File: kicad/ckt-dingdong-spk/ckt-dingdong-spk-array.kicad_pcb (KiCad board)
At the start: 2 copper layers, 40.6 x 180.3 mm, 170 parts, among them J1 Conn_01x02_MountingPin

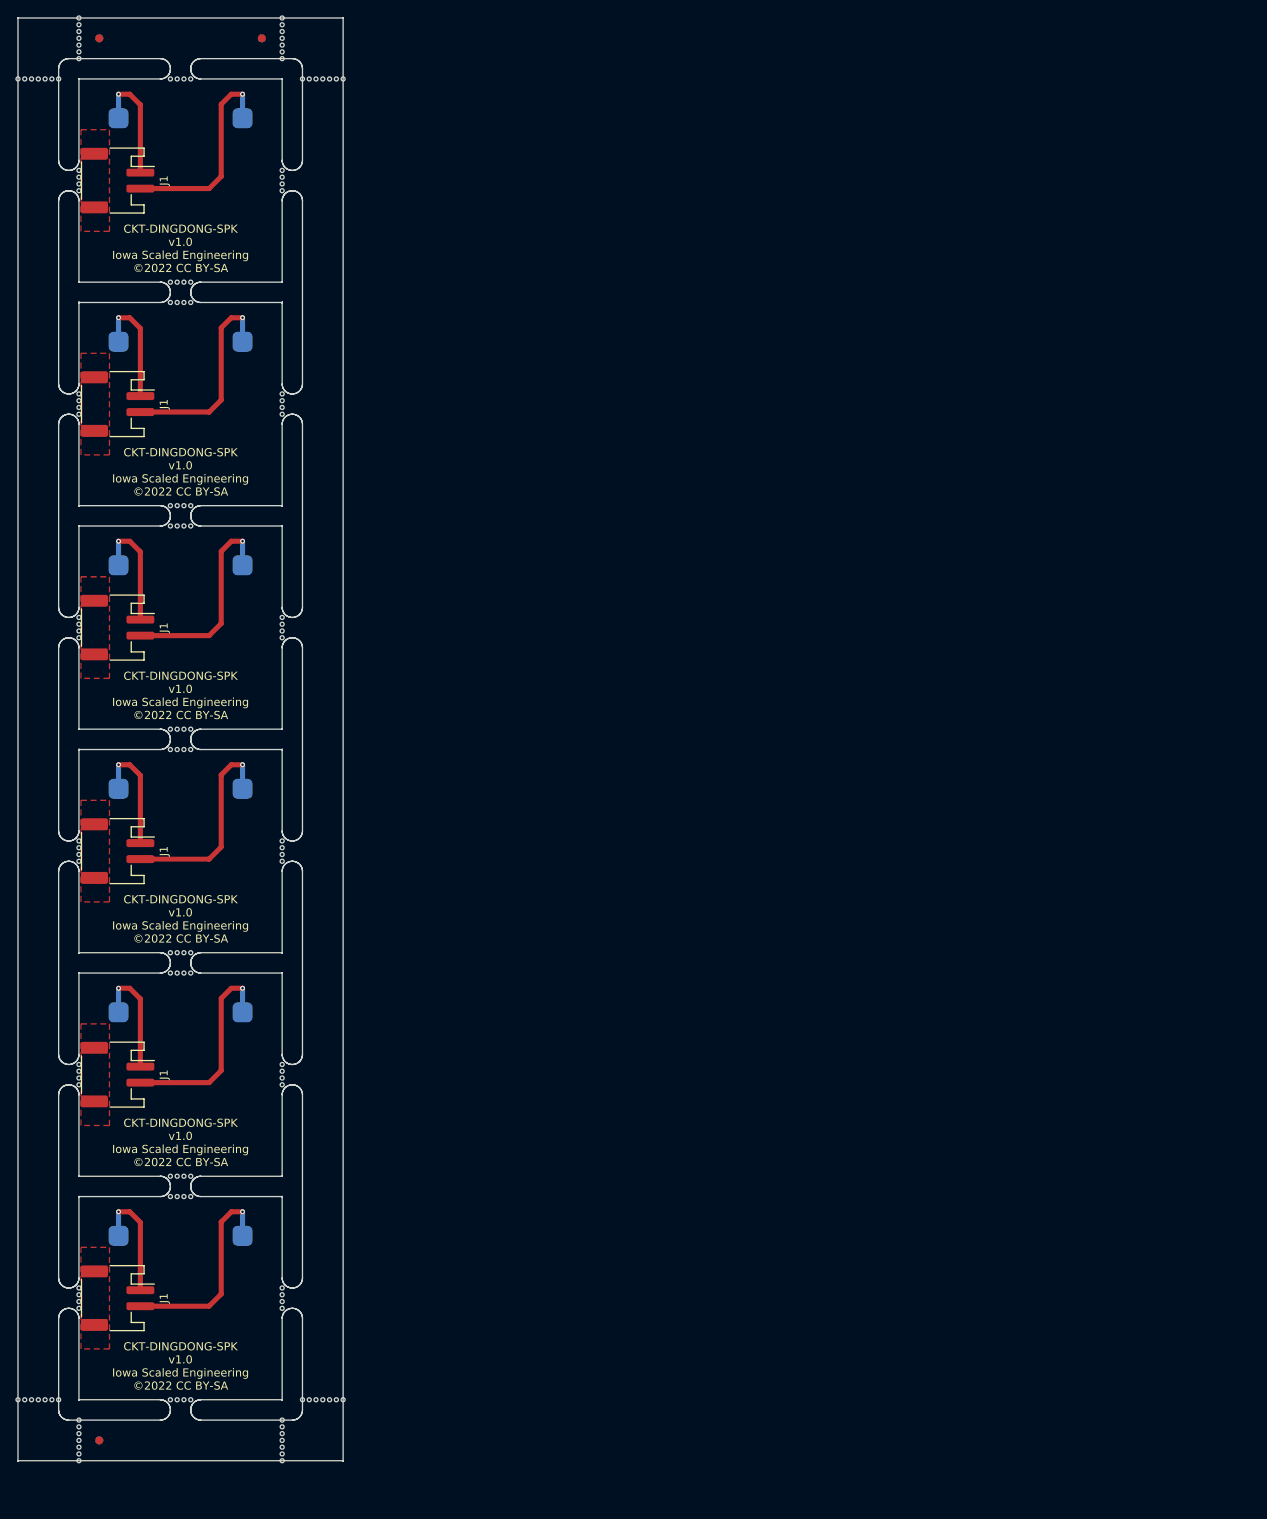
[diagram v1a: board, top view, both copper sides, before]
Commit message: Updated array with v2 board
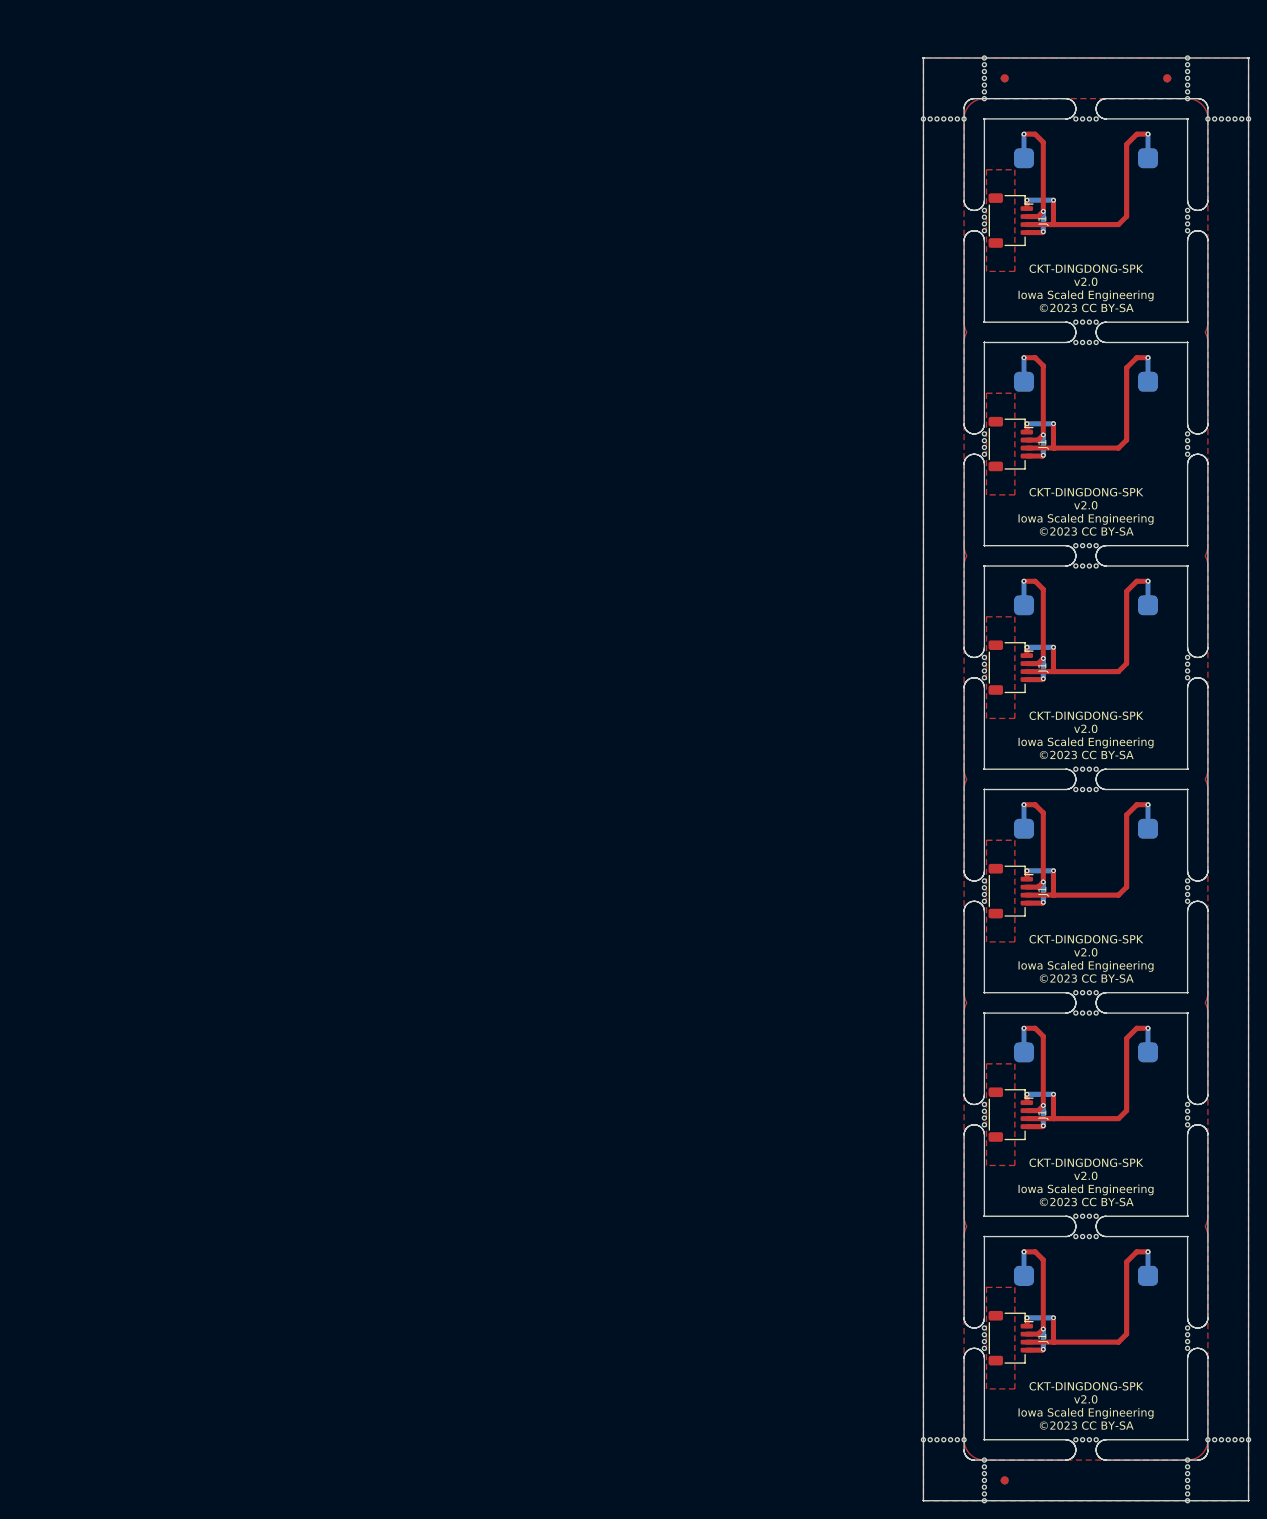
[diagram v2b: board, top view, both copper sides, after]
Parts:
- removed the J1 at (27.4, 35.3)
- removed the J1 at (27.4, 63.3)
- removed the J1 at (27.4, 147.1)
- removed the J1 at (27.4, 119.1)
- removed the J1 at (27.4, 175.0)
- removed the J1 at (27.4, 91.2)
- removed the REF** at (20.1, 22.6)
- removed the REF** at (53.9, 187.7)
- removed the REF** at (34.9, 134.4)
- removed the REF** at (45.5, 17.5) (x2)
- removed the REF** at (34.9, 76.0)
- removed the REF** at (34.9, 48.0)
- removed the REF** at (36.6, 48.0)
- removed the REF** at (52.3, 22.6)
- removed the REF** at (22.6, 194.5)
- removed the REF** at (22.6, 118.7)
- removed the REF** at (35.7, 187.7)
- removed the REF** at (48.0, 191.1)
- removed the REF** at (22.6, 147.5)
- removed the REF** at (55.6, 187.7)
- removed the REF** at (48.0, 194.5)
- removed the REF** at (36.6, 162.3)
- removed the REF** at (17.5, 22.6)
- removed the REF** at (36.6, 22.6)
- removed the REF** at (34.9, 106.4)
- removed the REF** at (48.0, 120.4)
- removed the REF** at (48.0, 18.4)
- removed the REF** at (34.0, 134.4)
- removed the REF** at (22.6, 36.6)
- removed the REF** at (22.6, 92.5)
- removed the REF** at (17.5, 187.7)
- removed the REF** at (48.0, 192.0)
- removed the REF** at (22.6, 34.0)
- removed the REF** at (53.9, 22.6)
- removed the REF** at (19.2, 187.7)
- removed the REF** at (34.0, 159.8)
- removed the REF** at (36.6, 50.6)
- removed the REF** at (22.6, 174.6)
- removed the REF** at (48.0, 90.8)
- removed the REF** at (22.6, 191.1)
- removed the REF** at (34.9, 159.8)
- removed the REF** at (18.4, 22.6)
- removed the REF** at (15.0, 187.7)
- removed the REF** at (22.6, 146.7)
- removed the REF** at (34.9, 187.7)
- removed the REF** at (22.6, 62.0)
- removed the REF** at (15.8, 22.6)
- removed the REF** at (34.9, 131.8)
- removed the REF** at (48.0, 92.5)
- removed the REF** at (22.6, 34.9)
- removed the REF** at (36.6, 78.5)
- removed the REF** at (35.7, 22.6)
- removed the REF** at (22.6, 119.6)
- removed the REF** at (22.6, 175.4)
- removed the REF** at (48.0, 15.0)
- removed the REF** at (35.7, 50.6)
- removed the REF** at (50.6, 22.6)
- removed the REF** at (22.6, 18.4)
- removed the REF** at (48.0, 190.3)
- removed the REF** at (35.7, 78.5)
- removed the REF** at (19.2, 22.6)
- removed the REF** at (34.0, 106.4)
- removed the REF** at (51.4, 187.7)
- removed the REF** at (48.0, 176.3)
- removed the REF** at (22.6, 176.3)
- removed the REF** at (34.9, 50.6)
- removed the REF** at (34.0, 50.6)
- removed the REF** at (22.6, 35.7)
- removed the REF** at (36.6, 159.8)
- removed the REF** at (25.2, 192.8) (x2)
- removed the REF** at (25.2, 17.5) (x2)
- removed the REF** at (36.6, 106.4)
- removed the REF** at (34.9, 78.5)
- removed the REF** at (35.7, 131.8)
- removed the REF** at (48.0, 35.7)
- removed the REF** at (35.7, 48.0)
- removed the REF** at (35.7, 162.3)
- removed the REF** at (48.0, 20.1)
- removed the REF** at (48.0, 147.5)
- removed the REF** at (22.6, 120.4)
- removed the REF** at (34.0, 78.5)
- removed the REF** at (22.6, 195.3)
- removed the REF** at (52.3, 187.7)
- removed the REF** at (36.6, 76.0)
- removed the REF** at (22.6, 15.8)
- removed the REF** at (16.7, 22.6)
- removed the REF** at (22.6, 193.6)
- removed the REF** at (15.8, 187.7)
- removed the REF** at (15.0, 22.6)
- removed the REF** at (48.0, 17.5)
- removed the REF** at (48.0, 118.7)
- removed the REF** at (54.8, 187.7)
- removed the REF** at (16.7, 187.7)
- removed the REF** at (22.6, 19.2)
- removed the REF** at (48.0, 62.8)
- removed the REF** at (22.6, 15.0)
- removed the REF** at (48.0, 64.5)
- removed the REF** at (20.1, 187.7)
- removed the REF** at (53.1, 22.6)
- removed the REF** at (22.6, 64.5)
- removed the REF** at (48.0, 36.6)
- removed the REF** at (36.6, 131.8)
- removed the REF** at (48.0, 173.8)
- removed the REF** at (36.6, 187.7)
- removed the REF** at (35.7, 106.4)
- removed the REF** at (22.6, 63.7)
- removed the REF** at (36.6, 103.9)
- removed the REF** at (35.7, 159.8)
- removed the REF** at (22.6, 192.0)
- removed the REF** at (48.0, 148.3)
- removed the REF** at (22.6, 91.6)
- removed the REF** at (22.6, 62.8)
- removed the REF** at (54.8, 22.6)
- removed the REF** at (48.0, 62.0)
- removed the REF** at (34.0, 22.6)
- removed the REF** at (48.0, 16.7)
- removed the REF** at (34.0, 162.3)
- removed the REF** at (48.0, 34.0)
- removed the REF** at (34.0, 103.9)
- removed the REF** at (36.6, 134.4)
- removed the REF** at (48.0, 34.9)
- removed the REF** at (48.0, 89.9)
- removed the REF** at (35.7, 134.4)
- removed the REF** at (48.0, 19.2)
- removed the REF** at (34.0, 76.0)
- removed the REF** at (18.4, 187.7)
- removed the REF** at (34.0, 187.7)
- removed the REF** at (22.6, 145.8)
- removed the REF** at (50.6, 187.7)
- removed the REF** at (35.7, 103.9)
- removed the REF** at (22.6, 17.5)
- removed the REF** at (48.0, 193.6)
- removed the REF** at (34.0, 48.0)
- removed the REF** at (48.0, 174.6)
- removed the REF** at (34.0, 131.8)
- removed the REF** at (35.7, 76.0)
- removed the REF** at (48.0, 119.6)
- removed the REF** at (22.6, 89.9)
- removed the REF** at (22.6, 192.8)
- removed the REF** at (48.0, 195.3)
- removed the REF** at (34.9, 22.6)
- removed the REF** at (48.0, 145.8)
- removed the REF** at (48.0, 63.7)
- removed the REF** at (22.6, 16.7)
- removed the REF** at (48.0, 15.8)
- removed the REF** at (22.6, 117.9)
- removed the REF** at (22.6, 173.8)
- removed the REF** at (53.1, 187.7)
- removed the REF** at (48.0, 91.6)
- removed the REF** at (22.6, 20.1)
- removed the REF** at (34.9, 103.9)
- removed the REF** at (34.9, 162.3)
- removed the REF** at (22.6, 148.3)
- removed the REF** at (48.0, 175.4)
- removed the REF** at (51.4, 22.6)
- removed the REF** at (48.0, 146.7)
- removed the REF** at (22.6, 190.3)
- removed the REF** at (55.6, 22.6)
- removed the REF** at (48.0, 117.9)
- removed the REF** at (48.0, 192.8)
- removed the REF** at (22.6, 90.8)
- removed the SPK1 at (35.3, 60.7)
- removed the SPK1 at (35.3, 116.6)
- removed the SPK1 at (35.3, 172.5)
- removed the SPK1 at (35.3, 32.8)
- removed the SPK1 at (35.3, 144.5)
- removed the SPK1 at (35.3, 88.7)
- added J1: SM04B-SRSS, Connector_JST:JST_SH_SM04B-SRSS-TB_1x04-1MP_P1.00mm_Horizontal, F.Cu at (139.1, 40.3)
- added J1: SM04B-SRSS, Connector_JST:JST_SH_SM04B-SRSS-TB_1x04-1MP_P1.00mm_Horizontal, F.Cu at (139.1, 152.1)
- added J1: SM04B-SRSS, Connector_JST:JST_SH_SM04B-SRSS-TB_1x04-1MP_P1.00mm_Horizontal, F.Cu at (139.1, 124.1)
- added J1: SM04B-SRSS, Connector_JST:JST_SH_SM04B-SRSS-TB_1x04-1MP_P1.00mm_Horizontal, F.Cu at (139.1, 180.0)
- added J1: SM04B-SRSS, Connector_JST:JST_SH_SM04B-SRSS-TB_1x04-1MP_P1.00mm_Horizontal, F.Cu at (139.1, 96.2)
- added J1: SM04B-SRSS, Connector_JST:JST_SH_SM04B-SRSS-TB_1x04-1MP_P1.00mm_Horizontal, F.Cu at (139.1, 68.3)
- added REF**: NPTH, NPTH, F.Cu at (129.0, 192.7)
- added REF**: NPTH, NPTH, F.Cu at (149.8, 139.4)
- added REF**: NPTH, NPTH, F.Cu at (148.1, 81.0)
- added REF**: NPTH, NPTH, F.Cu at (148.1, 192.7)
- added REF**: NPTH, NPTH, F.Cu at (161.2, 97.5)
- added REF**: NPTH, NPTH, F.Cu at (135.8, 69.5)
- added REF**: NPTH, NPTH, F.Cu at (130.7, 27.6)
- added REF**: NPTH, NPTH, F.Cu at (135.8, 180.4)
- added REF**: NPTH, NPTH, F.Cu at (161.2, 151.7)
- added REF**: NPTH, NPTH, F.Cu at (148.1, 164.8)
- added REF**: NPTH, NPTH, F.Cu at (135.8, 97.5)
- added REF**: NPTH, NPTH, F.Cu at (133.3, 192.7)
- added REF**: NPTH, NPTH, F.Cu at (166.3, 192.7)
- added REF**: NPTH, NPTH, F.Cu at (161.2, 180.4)
- added REF**: NPTH, NPTH, F.Cu at (161.2, 181.3)
- added REF**: NPTH, NPTH, F.Cu at (135.8, 200.3)
- added REF**: NPTH, NPTH, F.Cu at (147.2, 55.6)
- added REF**: NPTH, NPTH, F.Cu at (149.8, 167.3)
- added REF**: NPTH, NPTH, F.Cu at (163.7, 192.7)
- added REF**: NPTH, NPTH, F.Cu at (135.8, 20.8)
- added REF**: NPTH, NPTH, F.Cu at (161.2, 40.7)
- added REF**: NPTH, NPTH, F.Cu at (161.2, 21.7)
- added REF**: NPTH, NPTH, F.Cu at (165.4, 192.7)
- added REF**: NPTH, NPTH, F.Cu at (161.2, 152.5)
- added REF**: NPTH, NPTH, F.Cu at (135.8, 24.2)
- added REF**: NPTH, NPTH, F.Cu at (135.8, 198.6)
- added REF**: NPTH, NPTH, F.Cu at (148.1, 83.5)
- added REF**: NPTH, NPTH, F.Cu at (148.9, 27.6)
- added REF**: NPTH, NPTH, F.Cu at (168.0, 192.7)
- added REF**: NPTH, NPTH, F.Cu at (148.9, 83.5)
- added REF**: NPTH, NPTH, F.Cu at (129.9, 27.6)
- added REF**: NPTH, NPTH, F.Cu at (135.8, 125.4)
- added REF**: NPTH, NPTH, F.Cu at (133.3, 27.6)
- added REF**: NPTH, NPTH, F.Cu at (135.8, 151.7)
- added REF**: NPTH, NPTH, F.Cu at (147.2, 83.5)
- added REF**: NPTH, NPTH, F.Cu at (135.8, 94.9)
- added REF**: NPTH, NPTH, F.Cu at (161.2, 20.0)
- added REF**: NPTH, NPTH, F.Cu at (128.2, 27.6)
- added REF**: NPTH, NPTH, F.Cu at (161.2, 150.8)
- added REF**: NPTH, NPTH, F.Cu at (135.8, 41.6)
- added REF**: NPTH, NPTH, F.Cu at (167.1, 27.6)
- added REF**: NPTH, NPTH, F.Cu at (167.1, 192.7)
- added REF**: NPTH, NPTH, F.Cu at (149.8, 192.7)
- added REF**: NPTH, NPTH, F.Cu at (135.8, 124.6)
- added REF**: NPTH, NPTH, F.Cu at (168.8, 192.7)
- added REF**: NPTH, NPTH, F.Cu at (161.2, 179.6)
- added REF**: NPTH, NPTH, F.Cu at (148.1, 139.4)
- added REF**: NPTH, NPTH, F.Cu at (161.2, 124.6)
- added REF**: NPTH, NPTH, F.Cu at (131.6, 27.6)
- added REF**: NPTH, NPTH, F.Cu at (131.6, 192.7)
- added REF**: NPTH, NPTH, F.Cu at (148.1, 53.0)
- added REF**: NPTH, NPTH, F.Cu at (135.8, 122.9)
- added REF**: NPTH, NPTH, F.Cu at (149.8, 53.0)
- added REF**: NPTH, NPTH, F.Cu at (168.8, 27.6)
- added REF**: NPTH, NPTH, F.Cu at (135.8, 179.6)
- added REF**: NPTH, NPTH, F.Cu at (161.2, 25.1)
- added REF**: NPTH, NPTH, F.Cu at (164.6, 192.7)
- added REF**: NPTH, NPTH, F.Cu at (148.1, 167.3)
- added REF**: NPTH, NPTH, F.Cu at (135.8, 39.9)
- added REF**: Fiducial, Fiducial, F.Cu at (138.3, 22.5)
- added REF**: NPTH, NPTH, F.Cu at (163.7, 27.6)
- added REF**: NPTH, NPTH, F.Cu at (165.4, 27.6)
- added REF**: NPTH, NPTH, F.Cu at (161.2, 67.0)
- added REF**: Fiducial, Fiducial, B.Cu at (138.3, 197.8)
- added REF**: Fiducial, Fiducial, B.Cu at (138.3, 22.5)
- added REF**: Fiducial, Fiducial, B.Cu at (158.7, 22.5)
- added REF**: NPTH, NPTH, F.Cu at (161.2, 20.8)
- added REF**: NPTH, NPTH, F.Cu at (135.8, 178.8)
- added REF**: NPTH, NPTH, F.Cu at (135.8, 153.3)
- added REF**: NPTH, NPTH, F.Cu at (168.0, 27.6)
- added REF**: NPTH, NPTH, F.Cu at (147.2, 136.8)
- added REF**: NPTH, NPTH, F.Cu at (161.2, 68.7)
- added REF**: NPTH, NPTH, F.Cu at (135.8, 150.8)
- added REF**: NPTH, NPTH, F.Cu at (161.2, 196.1)
- added REF**: NPTH, NPTH, F.Cu at (166.3, 27.6)
- added REF**: NPTH, NPTH, F.Cu at (148.9, 164.8)
- added REF**: NPTH, NPTH, F.Cu at (147.2, 139.4)
- added REF**: NPTH, NPTH, F.Cu at (161.2, 199.5)
- added REF**: NPTH, NPTH, F.Cu at (135.8, 68.7)
- added REF**: NPTH, NPTH, F.Cu at (135.8, 20.0)
- added REF**: NPTH, NPTH, F.Cu at (147.2, 192.7)
- added REF**: NPTH, NPTH, F.Cu at (161.2, 39.9)
- added REF**: NPTH, NPTH, F.Cu at (161.2, 67.8)
- added REF**: NPTH, NPTH, F.Cu at (129.9, 192.7)
- added REF**: NPTH, NPTH, F.Cu at (161.2, 22.5)
- added REF**: NPTH, NPTH, F.Cu at (161.2, 24.2)
- added REF**: NPTH, NPTH, F.Cu at (161.2, 94.9)
- added REF**: NPTH, NPTH, F.Cu at (148.9, 192.7)
- added REF**: NPTH, NPTH, F.Cu at (135.8, 67.8)
- added REF**: NPTH, NPTH, F.Cu at (149.8, 136.8)
- added REF**: NPTH, NPTH, F.Cu at (135.8, 39.0)
- added REF**: NPTH, NPTH, F.Cu at (161.2, 125.4)
- added REF**: NPTH, NPTH, F.Cu at (135.8, 96.6)
- added REF**: NPTH, NPTH, F.Cu at (135.8, 181.3)
- added REF**: NPTH, NPTH, F.Cu at (129.0, 27.6)
- added REF**: NPTH, NPTH, F.Cu at (149.8, 55.6)
- added REF**: Fiducial, Fiducial, F.Cu at (138.3, 197.8)
- added REF**: NPTH, NPTH, F.Cu at (147.2, 167.3)
- added REF**: NPTH, NPTH, F.Cu at (132.4, 27.6)
- added REF**: NPTH, NPTH, F.Cu at (148.9, 136.8)
- added REF**: NPTH, NPTH, F.Cu at (135.8, 195.3)
- added REF**: NPTH, NPTH, F.Cu at (149.8, 81.0)
- added REF**: NPTH, NPTH, F.Cu at (161.2, 69.5)
- added REF**: NPTH, NPTH, F.Cu at (161.2, 197.0)
- added REF**: NPTH, NPTH, F.Cu at (149.8, 83.5)
- added REF**: NPTH, NPTH, F.Cu at (161.2, 96.6)
- added REF**: NPTH, NPTH, F.Cu at (161.2, 39.0)
- added REF**: NPTH, NPTH, F.Cu at (148.1, 136.8)
- added REF**: NPTH, NPTH, F.Cu at (161.2, 41.6)
- added REF**: NPTH, NPTH, F.Cu at (135.8, 40.7)
- added REF**: NPTH, NPTH, F.Cu at (147.2, 108.9)
- added REF**: NPTH, NPTH, F.Cu at (161.2, 195.3)
- added REF**: NPTH, NPTH, F.Cu at (135.8, 22.5)
- added REF**: NPTH, NPTH, F.Cu at (148.9, 108.9)
- added REF**: NPTH, NPTH, F.Cu at (128.2, 192.7)
- added REF**: NPTH, NPTH, F.Cu at (148.1, 27.6)
- added REF**: NPTH, NPTH, F.Cu at (149.8, 164.8)
- added REF**: NPTH, NPTH, F.Cu at (161.2, 122.9)
- added REF**: NPTH, NPTH, F.Cu at (135.8, 21.7)
- added REF**: NPTH, NPTH, F.Cu at (147.2, 81.0)
- added REF**: NPTH, NPTH, F.Cu at (161.2, 178.8)
- added REF**: NPTH, NPTH, F.Cu at (135.8, 199.5)
- added REF**: NPTH, NPTH, F.Cu at (161.2, 200.3)
- added REF**: NPTH, NPTH, F.Cu at (148.9, 81.0)
- added REF**: NPTH, NPTH, F.Cu at (135.8, 23.4)
- added REF**: NPTH, NPTH, F.Cu at (161.2, 95.8)
- added REF**: NPTH, NPTH, F.Cu at (148.9, 53.0)
- added REF**: NPTH, NPTH, F.Cu at (149.8, 108.9)
- added REF**: NPTH, NPTH, F.Cu at (135.8, 197.0)
- added REF**: NPTH, NPTH, F.Cu at (148.1, 55.6)
- added REF**: NPTH, NPTH, F.Cu at (135.8, 197.8)
- added REF**: NPTH, NPTH, F.Cu at (164.6, 27.6)
- added REF**: NPTH, NPTH, F.Cu at (148.1, 108.9)
- added REF**: NPTH, NPTH, F.Cu at (135.8, 196.1)
- added REF**: NPTH, NPTH, F.Cu at (147.2, 164.8)
- added REF**: NPTH, NPTH, F.Cu at (148.9, 111.4)
- added REF**: NPTH, NPTH, F.Cu at (161.2, 197.8)
- added REF**: NPTH, NPTH, F.Cu at (161.2, 153.3)
- added REF**: NPTH, NPTH, F.Cu at (148.9, 167.3)
- added REF**: Fiducial, Fiducial, F.Cu at (158.7, 22.5)
- added REF**: NPTH, NPTH, F.Cu at (147.2, 53.0)
- added REF**: NPTH, NPTH, F.Cu at (135.8, 152.5)
- added REF**: NPTH, NPTH, F.Cu at (135.8, 25.1)
- added REF**: NPTH, NPTH, F.Cu at (147.2, 27.6)
- added REF**: NPTH, NPTH, F.Cu at (130.7, 192.7)
- added REF**: NPTH, NPTH, F.Cu at (161.2, 23.4)
- added REF**: NPTH, NPTH, F.Cu at (161.2, 123.7)
- added REF**: NPTH, NPTH, F.Cu at (132.4, 192.7)
- added REF**: NPTH, NPTH, F.Cu at (135.8, 123.7)
- added REF**: NPTH, NPTH, F.Cu at (147.2, 111.4)
- added REF**: NPTH, NPTH, F.Cu at (149.8, 111.4)
- added REF**: NPTH, NPTH, F.Cu at (148.9, 139.4)
- added REF**: NPTH, NPTH, F.Cu at (148.9, 55.6)
- added REF**: NPTH, NPTH, F.Cu at (161.2, 198.6)
- added REF**: NPTH, NPTH, F.Cu at (135.8, 67.0)
- added REF**: NPTH, NPTH, F.Cu at (149.8, 27.6)
- added REF**: NPTH, NPTH, F.Cu at (135.8, 95.8)
- added REF**: NPTH, NPTH, F.Cu at (148.1, 111.4)
- added SPK1: Speaker, ISE_Generic:Speaker_13x18, B.Cu at (148.5, 121.6)
- added SPK1: Speaker, ISE_Generic:Speaker_13x18, B.Cu at (148.5, 37.8)
- added SPK1: Speaker, ISE_Generic:Speaker_13x18, B.Cu at (148.5, 93.7)
- added SPK1: Speaker, ISE_Generic:Speaker_13x18, B.Cu at (148.5, 65.7)
- added SPK1: Speaker, ISE_Generic:Speaker_13x18, B.Cu at (148.5, 177.5)
- added SPK1: Speaker, ISE_Generic:Speaker_13x18, B.Cu at (148.5, 149.5)
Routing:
- net Board_5-Net-(SPK1-Pad1): track 25.9 -> 35.5 mm, vias 1 -> 3
- net Board_4-Net-(SPK1-Pad1): track 25.9 -> 35.5 mm, vias 1 -> 3
- net Board_2-Net-(SPK1-Pad1): track 25.9 -> 35.5 mm, vias 1 -> 3
- net Board_3-Net-(SPK1-Pad1): track 25.9 -> 35.5 mm, vias 1 -> 3
- net Board_1-Net-(SPK1-Pad1): track 25.9 -> 35.5 mm, vias 1 -> 3
- net Board_0-Net-(SPK1-Pad1): track 25.9 -> 35.5 mm, vias 1 -> 3
- net Board_3-Net-(SPK1-Pad2): track 14.7 -> 21.5 mm, vias 1 -> 3
- net Board_1-Net-(SPK1-Pad2): track 14.7 -> 21.5 mm, vias 1 -> 3
- net Board_4-Net-(SPK1-Pad2): track 14.7 -> 21.5 mm, vias 1 -> 3
- net Board_0-Net-(SPK1-Pad2): track 14.7 -> 21.5 mm, vias 1 -> 3
- net Board_2-Net-(SPK1-Pad2): track 14.7 -> 21.5 mm, vias 1 -> 3
- net Board_5-Net-(SPK1-Pad2): track 14.7 -> 21.5 mm, vias 1 -> 3
- added copper zone on F.Cu, net (none)
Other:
- board text added: "CKT-DINGDONG-SPK v2.0 Iowa Scaled Engineering ©2023 CC BY-SA"
- board text removed: "CKT-DINGDONG-SPK v1.0 Iowa Scaled Engineering ©2022 CC BY-SA"
